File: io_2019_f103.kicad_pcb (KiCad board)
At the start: 2 copper layers, 69.5 x 90.2 mm, 48 parts, among them J1 Con_Tirette, J10 Con_EV, J11 Con_EV, J12 Con_EV, J13 Con_EV, J2 Conn_01x04, J3 Conn_01x20_Female, J4 Alim logique, J5 Conn_01x20_Female, J7 Con_Buzzer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

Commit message: fix the pcb
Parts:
- moved Q5 0.98 mm to (109.2, 63.6), turned to 90 degrees
- moved Q10 0.98 mm to (109.2, 111.7), turned to 90 degrees
- moved Q6 0.97 mm to (109.2, 73.2), turned to 90 degrees
- moved Q9 0.97 mm to (109.2, 102.0), turned to 90 degrees
- moved Q7 0.97 mm to (109.2, 82.8), turned to 90 degrees
- moved Q8 0.97 mm to (109.2, 92.4), turned to 90 degrees
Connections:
- D10 pad 1: GND -> Net-(D10-Pad1)
- D5 pad 1: GND -> Net-(D5-Pad1)
- D6 pad 1: GND -> Net-(D6-Pad1)
- D7 pad 1: GND -> Net-(D7-Pad1)
- D8 pad 1: GND -> Net-(D8-Pad1)
- D9 pad 1: GND -> Net-(D9-Pad1)
- J10 pad 1: Net-(J10-Pad1) -> Net-(D7-Pad1)
- J11 pad 1: Net-(J11-Pad1) -> Net-(D8-Pad1)
- J12 pad 1: Net-(J12-Pad1) -> Net-(D9-Pad1)
- J13 pad 1: Net-(J13-Pad1) -> Net-(D10-Pad1)
- J8 pad 1: Net-(J8-Pad1) -> Net-(D5-Pad1)
- J9 pad 1: Net-(J9-Pad1) -> Net-(D6-Pad1)
- Q10 pad 2: Net-(J13-Pad1) -> GND
- Q10 pad 3: +5V -> Net-(D10-Pad1)
- Q5 pad 2: Net-(J8-Pad1) -> GND
- Q5 pad 3: +5V -> Net-(D5-Pad1)
- Q6 pad 2: Net-(J9-Pad1) -> GND
- Q6 pad 3: +5V -> Net-(D6-Pad1)
- Q7 pad 2: Net-(J10-Pad1) -> GND
- Q7 pad 3: +5V -> Net-(D7-Pad1)
- Q8 pad 2: Net-(J11-Pad1) -> GND
- Q8 pad 3: +5V -> Net-(D8-Pad1)
- Q9 pad 2: Net-(J12-Pad1) -> GND
- Q9 pad 3: +5V -> Net-(D9-Pad1)
- R10 pad 2: Net-(J11-Pad1) -> +5V
- R11 pad 2: Net-(J12-Pad1) -> +5V
- R12 pad 2: Net-(J13-Pad1) -> +5V
- R7 pad 2: Net-(J8-Pad1) -> +5V
- R8 pad 2: Net-(J9-Pad1) -> +5V
- R9 pad 2: Net-(J10-Pad1) -> +5V
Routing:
- net +5V: track 327.5 -> 135.3 mm
- net GND: track 44.9 -> 95.5 mm
- net Net-(D5-Pad1): track 0.00 -> 14.6 mm
- net Net-(D6-Pad1): track 0.00 -> 14.6 mm
- net Net-(D9-Pad1): track 0.00 -> 14.5 mm
- net Net-(D7-Pad1): track 0.00 -> 14.5 mm
- net Net-(D8-Pad1): track 0.00 -> 14.4 mm
- net Net-(D10-Pad1): track 0.00 -> 14.3 mm
- net Net-(J12-Pad1): track 10.5 -> 0.00 mm
- net Net-(J10-Pad1): track 10.3 -> 0.00 mm
- net Net-(J11-Pad1): track 10.2 -> 0.00 mm
- net Net-(J8-Pad1): track 9.92 -> 0.00 mm
- net Net-(J9-Pad1): track 9.91 -> 0.00 mm
- net Net-(J13-Pad1): track 9.60 -> 0.00 mm
- net /EV3: track 12.2 -> 7.57 mm
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
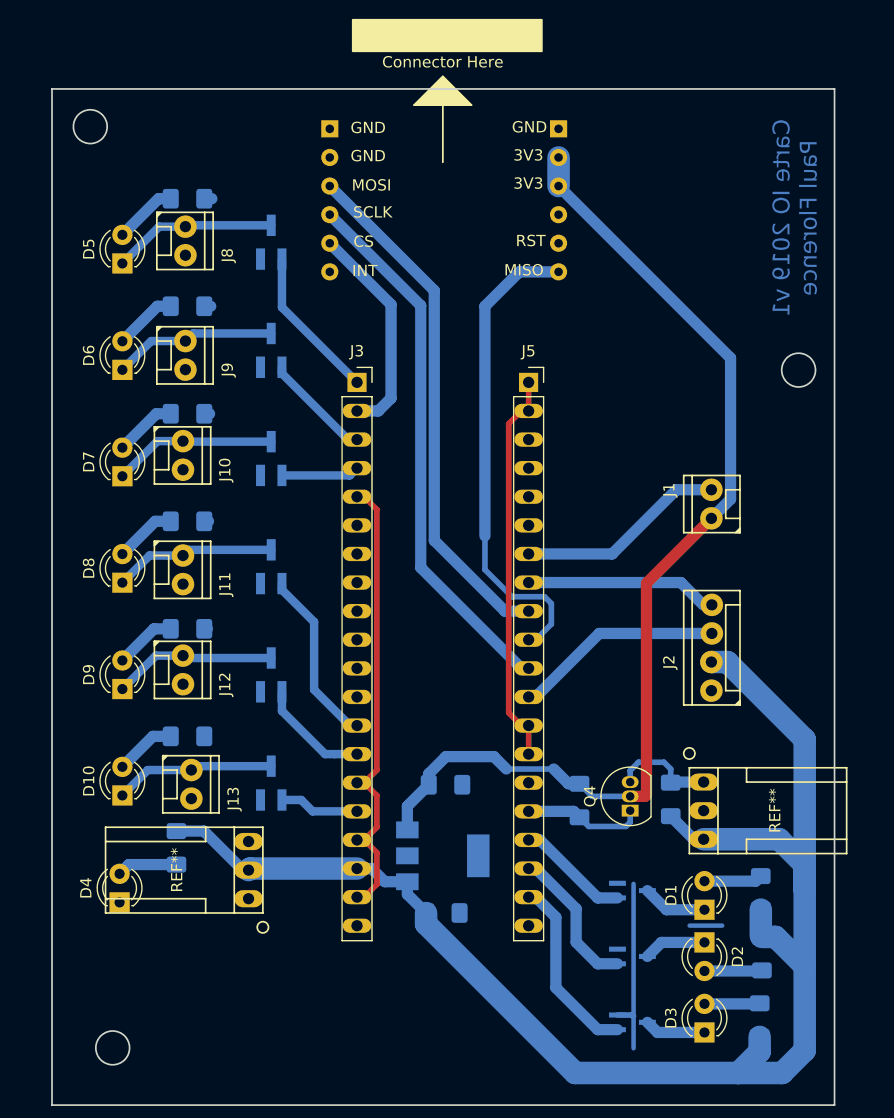
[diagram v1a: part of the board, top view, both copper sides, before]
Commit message: Update pcb to take into account fixes made by @dotsumae
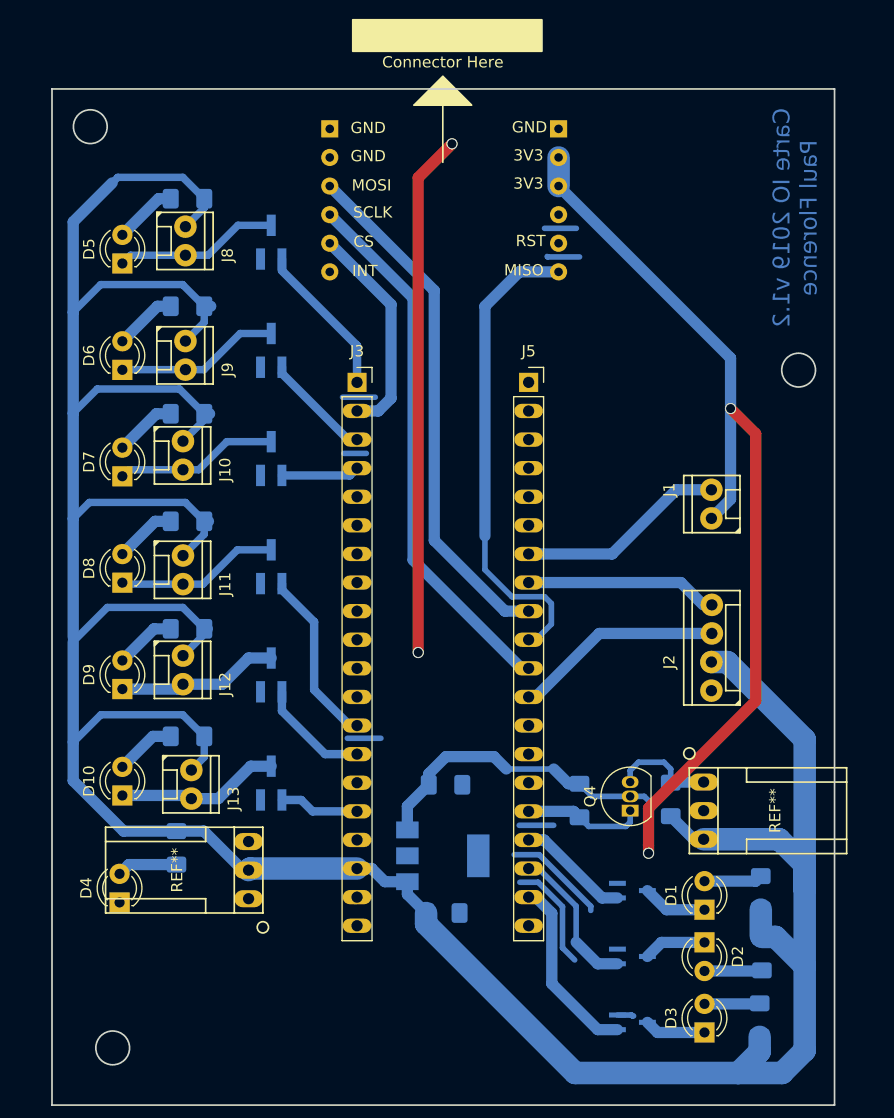
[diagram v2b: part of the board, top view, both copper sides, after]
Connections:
- J10 pad 1: Net-(D7-Pad1) -> +5V
- J10 pad 2: GND -> Net-(D7-Pad1)
- J11 pad 1: Net-(D8-Pad1) -> +5V
- J11 pad 2: GND -> Net-(D8-Pad1)
- J12 pad 1: Net-(D9-Pad1) -> +5V
- J12 pad 2: GND -> Net-(D9-Pad1)
- J13 pad 1: Net-(D10-Pad1) -> +5V
- J13 pad 2: GND -> Net-(D10-Pad1)
- J8 pad 1: Net-(D5-Pad1) -> +5V
- J8 pad 2: GND -> Net-(D5-Pad1)
- J9 pad 1: Net-(D6-Pad1) -> +5V
- J9 pad 2: GND -> Net-(D6-Pad1)
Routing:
- net +5V: track 135.3 -> 296.9 mm
- net +3V3: track 93.3 -> 115.5 mm, vias 0 -> 2
- net GND: track 95.5 -> 87.5 mm, vias 0 -> 2
- net /led_communication: track 13.1 -> 13.9 mm
- net Net-(D10-Pad1): track 14.3 -> 14.9 mm
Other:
- board text added: "Carte IO 2019 v1.2 Paul Florence"
- board text removed: "Carte IO 2019 v1 Paul Florence"

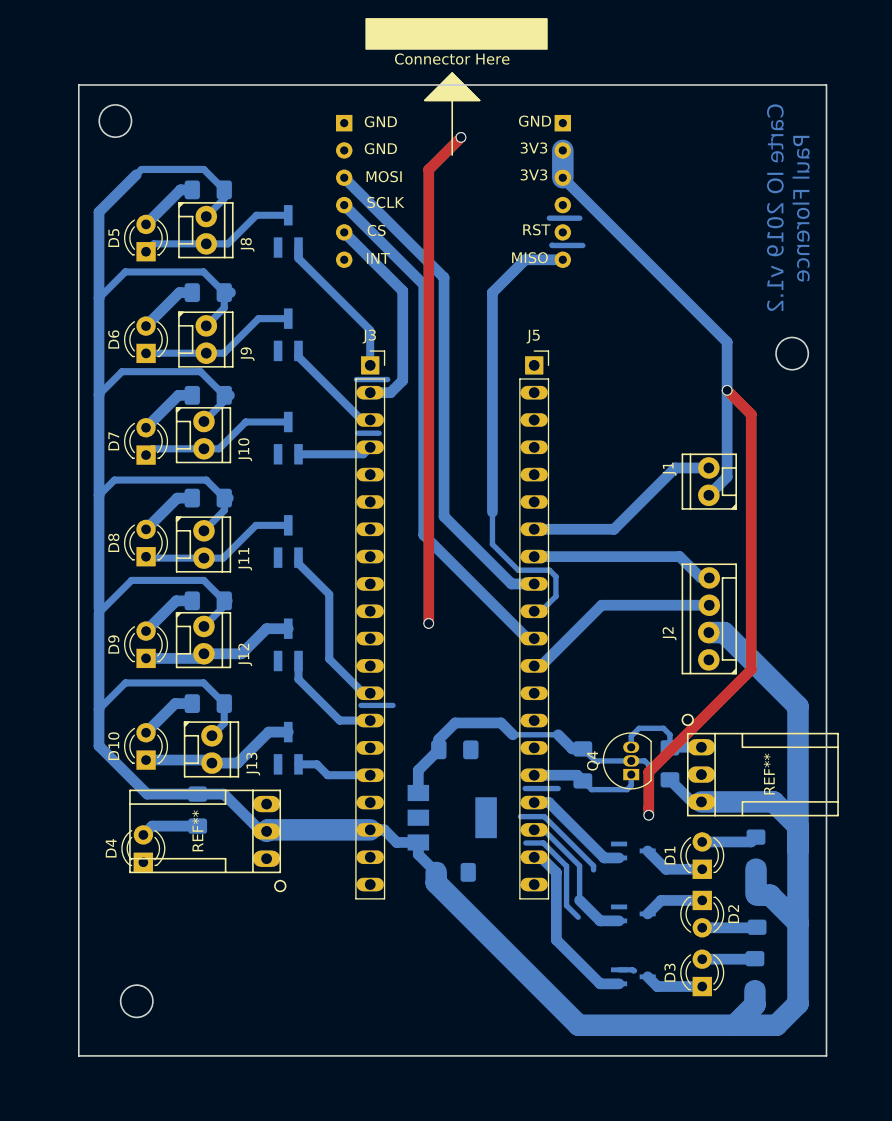
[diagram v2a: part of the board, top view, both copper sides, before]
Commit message: Add a little bit of margin on the side of the PCB Scale up vias copper pad so that it will be easier to solder
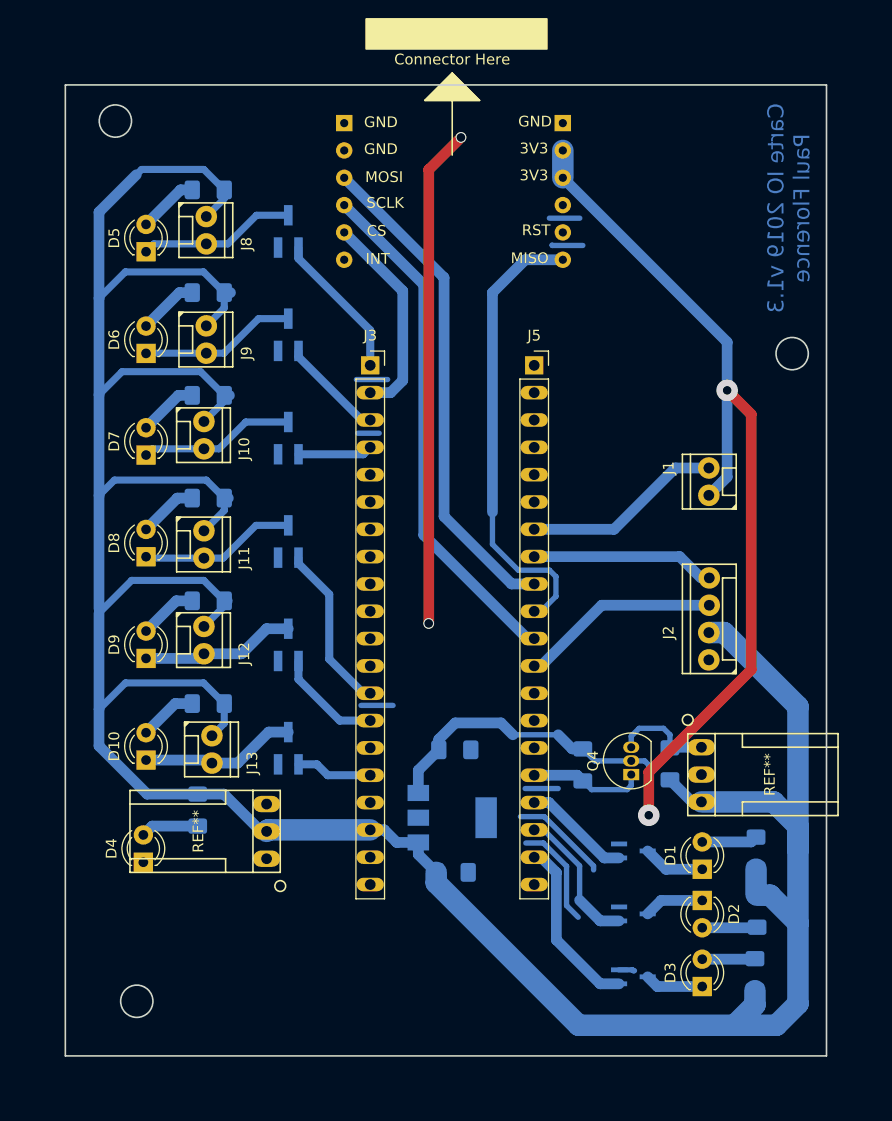
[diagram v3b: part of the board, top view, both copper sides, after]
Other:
- board size 69.5 x 90.2 mm -> 70.8 x 90.2 mm
- board text added: "Carte IO 2019 v1.3 Paul Florence"
- board text removed: "Carte IO 2019 v1.2 Paul Florence"
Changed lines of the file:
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@@
   (title_block
     (title "Carte IO/Pompe 2019")
-    (date 2019-05-11)
-    (rev v1.2)
+    (date 2019-05-13)
+    (rev v1.3)
     (company "Club Robot")
     (comment 1 Paul)
@@
   )
   (setup
-    (last_trace_width 1)
+    (last_trace_width 0.25)
     (user_trace_width 0.4)
     (user_trace_width 0.5)
@@
   (gr_circle (center 95.14 135.17) (end 96.64 135.17) (layer Edge.Cuts) (width 0.15))
   (gr_circle (center 93.15 53.35) (end 94.65 53.35) (layer Edge.Cuts) (width 0.15))
-  (gr_text "Carte IO 2019 v1.2\nPaul Florence" (at 155.76 61.45 90) (layer B.Cu)
+  (gr_text "Carte IO 2019 v1.3\nPaul Florence" (at 155.76 61.45 90) (layer B.Cu)
     (effects (font (size 1.5 1.5) (thickness 0.2)) (justify mirror))
   )
   (gr_line (start 159.25 50) (end 159.25 140.25) (layer Edge.Cuts) (width 0.15))
-  (gr_line (start 89.75 50) (end 159.25 50) (layer Edge.Cuts) (width 0.15))
-  (gr_line (start 89.75 140.25) (end 89.75 50) (layer Edge.Cuts) (width 0.15))
-  (gr_line (start 159.25 140.25) (end 89.75 140.25) (layer Edge.Cuts) (width 0.15))
+  (gr_line (start 88.5 50) (end 159.25 50) (layer Edge.Cuts) (width 0.15))
+  (gr_line (start 88.5 140.25) (end 88.5 50) (layer Edge.Cuts) (width 0.15))
+  (gr_line (start 159.25 140.25) (end 88.5 140.25) (layer Edge.Cuts) (width 0.15))
   (gr_line (start 127.635 130.175) (end 127.635 126.365) (layer Dwgs.User) (width 0.2))
   (gr_line (start 121.285 130.175) (end 127.635 130.175) (layer Dwgs.User) (width 0.2))
@@
   (gr_line (start 115.57 126.66) (end 133.57 126.66) (layer Dwgs.User) (width 0.2))
   (gr_line (start 115.57 73.66) (end 115.57 126.66) (layer Dwgs.User) (width 0.2))
-  (via (at 125.275 54.875) (size 1) (drill 0.8) (layers F.Cu B.Cu) (net 2))
-  (segment (start 135.09001 122.620575) (end 135.09001 126.28001) (width 0.5) (layer B.Cu) (net 2))
-  (segment (start 131.3 120.46) (end 132.929435 120.46) (width 0.5) (layer B.Cu) (net 2))
-  (segment (start 132.929435 120.46) (end 135.09001 122.620575) (width 0.5) (layer B.Cu) (net 2))
-  (segment (start 135.09001 126.28001) (end 136.17 127.36) (width 0.5) (layer B.Cu) (net 2))
   (segment (start 121.31 121.5275) (end 122.9725 123.19) (width 1) (layer B.Cu) (net 1) (status 20))
   (segment (start 121.31 120.41) (end 121.31 121.5275) (width 1) (layer B.Cu) (net 1) (status 10))
@@
   (segment (start 95.09499 58.34499) (end 95.58998 57.85) (width 0.66) (layer B.Cu) (net 1))
   (segment (start 95.58998 57.85) (end 101.371247 57.85) (width 0.66) (layer B.Cu) (net 1))
+  (via (at 125.275 54.875) (size 1) (drill 0.8) (layers F.Cu B.Cu) (net 2))
+  (segment (start 135.09001 122.620575) (end 135.09001 126.28001) (width 0.5) (layer B.Cu) (net 2))
+  (segment (start 131.3 120.46) (end 132.929435 120.46) (width 0.5) (layer B.Cu) (net 2))
+  (segment (start 132.929435 120.46) (end 135.09001 122.620575) (width 0.5) (layer B.Cu) (net 2))
+  (segment (start 135.09001 126.28001) (end 136.17 127.36) (width 0.5) (layer B.Cu) (net 2))
   (segment (start 116.7 121.92) (end 116.84 121.78) (width 1) (layer B.Cu) (net 2) (status 30))
-  (segment (start 101.58 74.95) (end 101.6 74.93) (width 1) (layer B.Cu) (net 53) (status 30))
-  (segment (start 101.252506 93.85) (end 101.382506 93.98) (width 1) (layer B.Cu) (net 55) (status 30))
   (segment (start 141.22 132.25) (end 141.304 132.334) (width 0.5) (layer B.Cu) (net 2))
   (segment (start 139.97 132.25) (end 141.22 132.25) (width 0.5) (layer B.Cu) (net 2) (status 10))
@@
   (segment (start 142.76 116.849999) (end 142.76 117.7) (width 0.5) (layer B.Cu) (net 3))
   (segment (start 150.015001 78.384999) (end 150.015001 86.439999) (width 1) (layer B.Cu) (net 3))
-  (via (at 150.015001 78.384999) (size 1) (drill 0.8) (layers F.Cu B.Cu) (net 3))
-  (via (at 142.73 117.88) (size 1) (drill 0.8) (layers F.Cu B.Cu) (net 3))
+  (via (at 150.015001 78.384999) (size 2) (drill 0.8) (layers F.Cu B.Cu) (net 3) (status 1000000))
+  (via (at 142.73 117.88) (size 2) (drill 0.8) (layers F.Cu B.Cu) (net 3))
   (segment (start 142.73 113.879406) (end 142.73 117.172894) (width 1) (layer F.Cu) (net 3))
   (segment (start 152.25 104.359406) (end 142.73 113.879406) (width 1) (layer F.Cu) (net 3))
@@
   (segment (start 103.605 64.77) (end 101.6 64.77) (width 0.66) (layer B.Cu) (net 52))
   (segment (start 106.265 62.11) (end 103.605 64.77) (width 0.66) (layer B.Cu) (net 52))
+  (segment (start 101.58 74.95) (end 101.6 74.93) (width 1) (layer B.Cu) (net 53) (status 30))
   (segment (start 96.02 74.93) (end 96 74.95) (width 0.66) (layer B.Cu) (net 53) (status 30))
   (segment (start 101.6 74.93) (end 96.02 74.93) (width 0.66) (layer B.Cu) (net 53) (status 30))
@@
   (segment (start 109.22 81.326) (end 105.274 81.326) (width 0.66) (layer B.Cu) (net 54))
   (segment (start 105.274 81.326) (end 102.78 83.82) (width 0.66) (layer B.Cu) (net 54))
+  (segment (start 101.252506 93.85) (end 101.382506 93.98) (width 1) (layer B.Cu) (net 55) (status 30))
   (segment (start 96.13 93.98) (end 96 93.85) (width 0.66) (layer B.Cu) (net 55) (status 30))
   (segment (start 101.382506 93.98) (end 96.13 93.98) (width 0.66) (layer B.Cu) (net 55) (status 30))

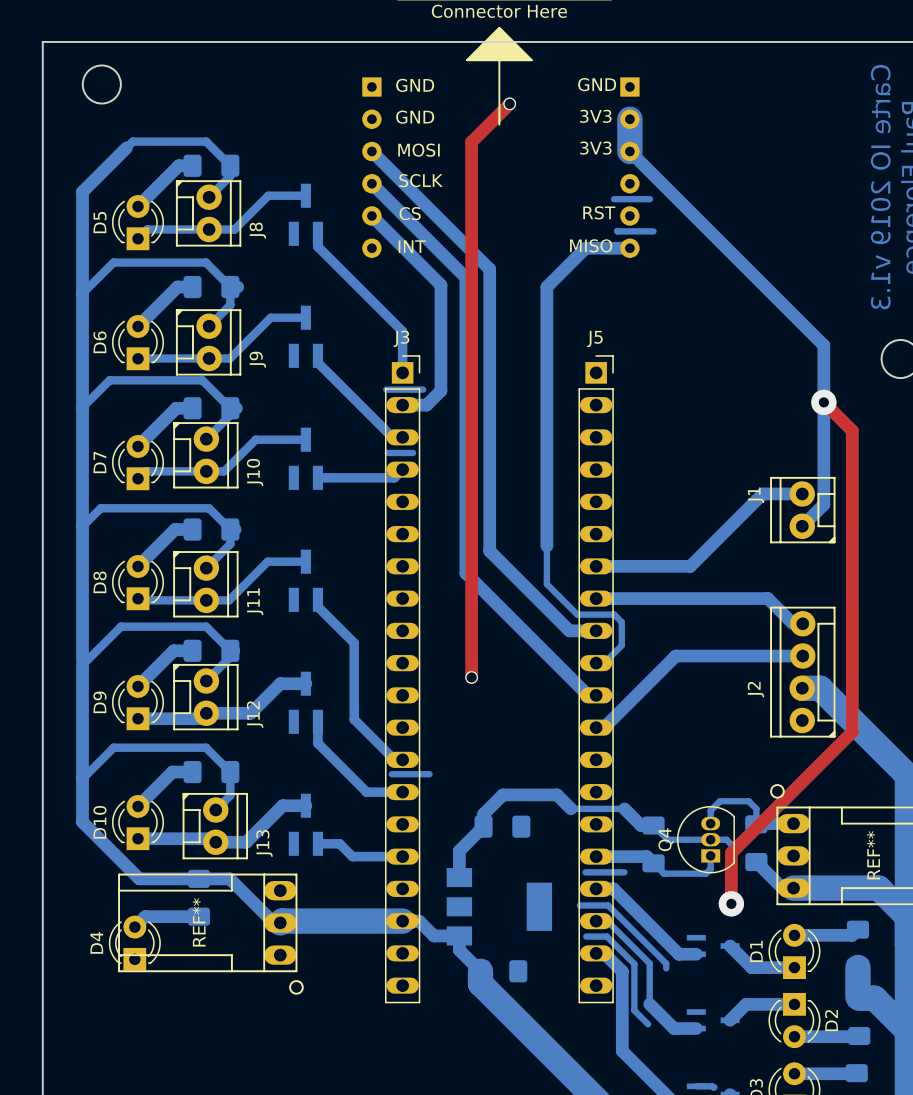
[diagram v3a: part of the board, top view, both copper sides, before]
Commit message: Update connector footprint
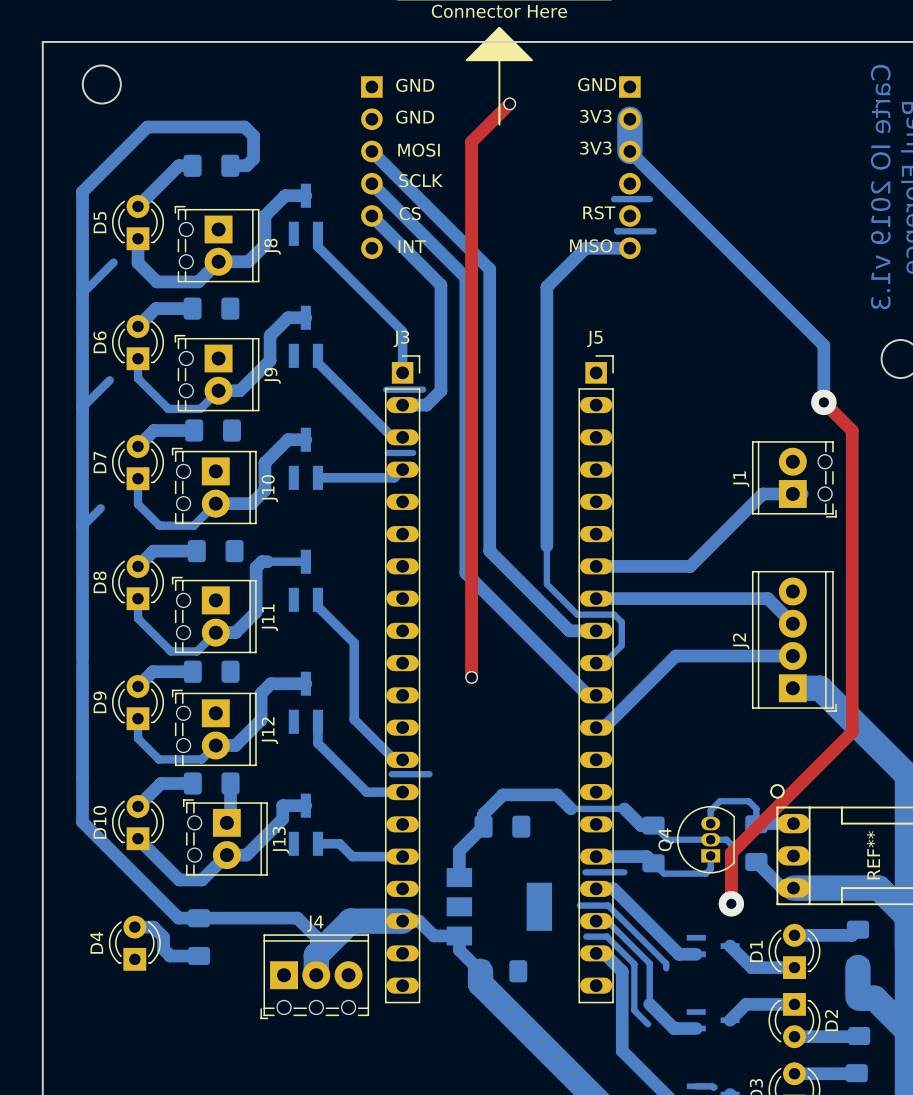
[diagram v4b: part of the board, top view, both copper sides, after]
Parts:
- J1, J10, J11, J12, J13, J8, J9: footprint @Robot:HE14-2-straight -> TerminalBlock_Phoenix:TerminalBlock_Phoenix_MPT-0,5-2-2.54_1x02_P2.54mm_Horizontal
- J2: footprint @Robot:HE14-4-straight -> TerminalBlock_Phoenix:TerminalBlock_Phoenix_MPT-0,5-4-2.54_1x04_P2.54mm_Horizontal
- J4: footprint @Robot:HE14-3_horizontal -> TerminalBlock_Phoenix:TerminalBlock_Phoenix_MPT-0,5-3-2.54_1x03_P2.54mm_Horizontal
- moved J4 5.82 mm to (107.5, 123.5), turned to 0 degrees
- moved R5 3.10 mm to (100.8, 120.5)
- moved R9 1.75 mm to (101.9, 80.6)
- moved R10 1.73 mm to (102.1, 90.1)
- moved R8 1.70 mm to (101.8, 71.0)
- moved R11 1.65 mm to (101.8, 99.6)
- moved J13 1.54 mm to (103.0, 111.5)
- moved R12 0.90 mm to (101.8, 108.4)
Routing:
- net +5V: track 296.9 -> 230.8 mm
- net +3V3: track 115.5 -> 105.0 mm
- net Net-(D7-Pad1): track 14.5 -> 20.8 mm
- net Net-(D8-Pad1): track 14.7 -> 21.0 mm
- net Net-(D6-Pad1): track 14.6 -> 19.9 mm
- net Net-(D5-Pad1): track 14.6 -> 19.9 mm
- net Net-(D9-Pad1): track 15.0 -> 19.8 mm
- net Net-(D10-Pad1): track 14.9 -> 18.0 mm
- net Net-(D4-Pad2): track 5.18 -> 7.00 mm
- net Net-(D6-Pad2): track 5.58 -> 4.88 mm
- net Net-(D9-Pad2): track 5.46 -> 4.79 mm
- net Net-(D7-Pad2): track 5.54 -> 4.95 mm
